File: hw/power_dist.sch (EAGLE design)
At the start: 78 parts, among them J1 JST-ZH6SMT_VERT, J2 JST-PH4SMT_VERT, J3 JST-PH5VERT, P1 XT30P, P2 XT30P, P3 XT30P, P4 XT30P, P5 XT30P, P6 XT30P, P7 XT90PW-M, Q1 PSMN4R8-100BSEJ, Q2 PSMN4R8-100BSEJ, Q3 PSMN4R8-100BSEJ, Q4 MF-DSC-SOT233-MMBT3904, Q5 MMBT5401 100V, U1 MAX15062AATA+T, U2 STM32G474CEU6, U4 TCAN334G, U5 LT1787HVIMS8PBF, U6 LTC4830

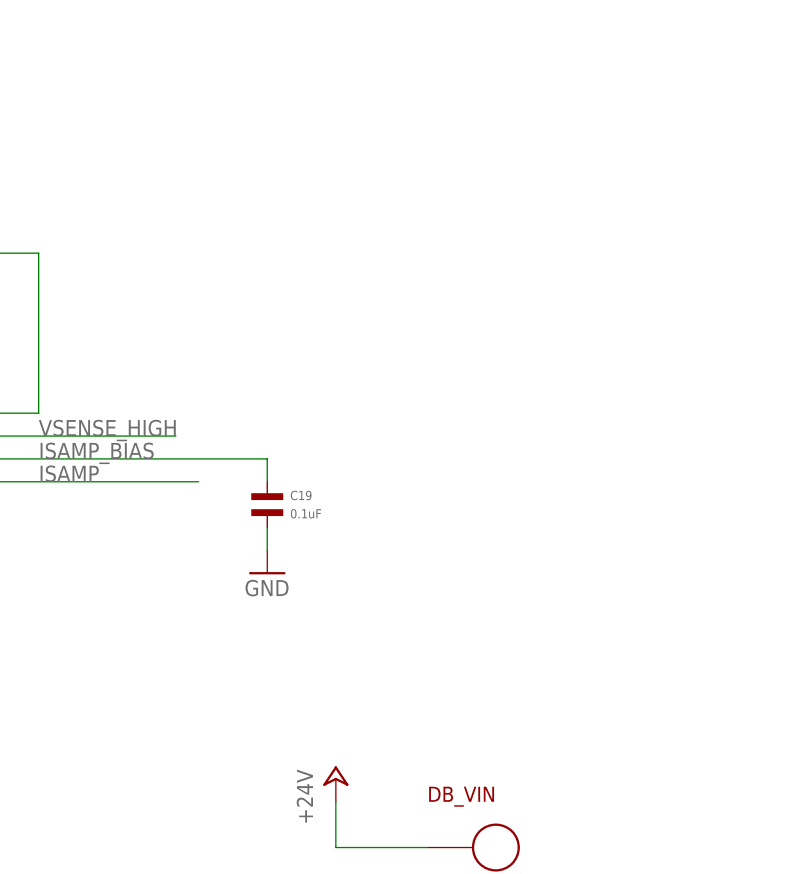
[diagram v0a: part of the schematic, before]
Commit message: Add more debugging pads
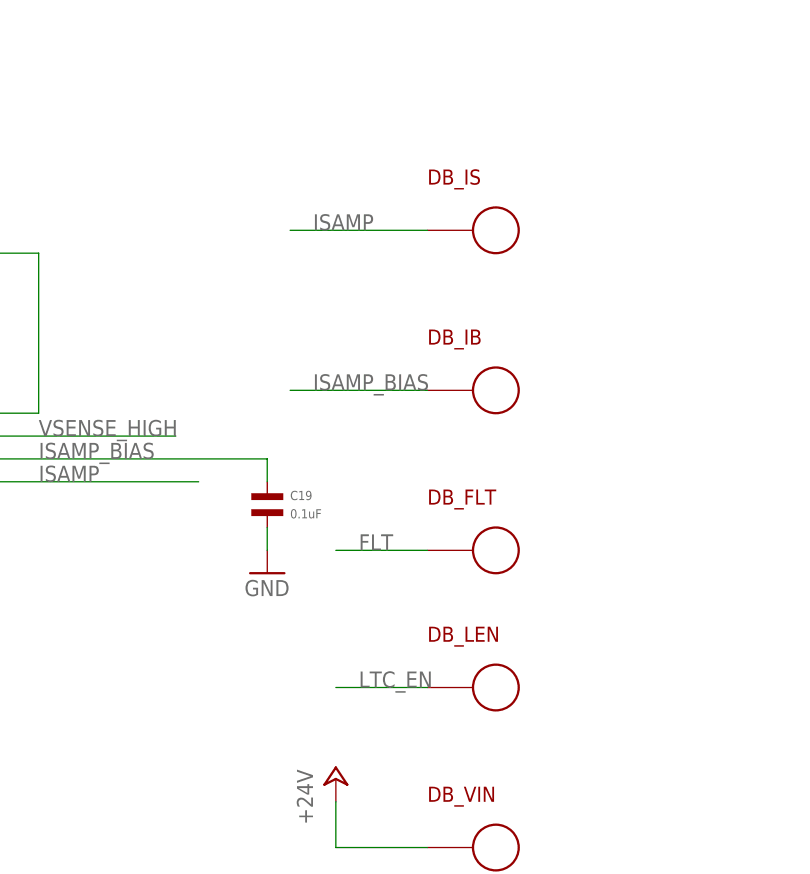
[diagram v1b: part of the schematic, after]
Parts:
- added DB_FLT, DB_IB, DB_IS, DB_LEN: PAD24AWG_PAD, precharge:PAD24AWG_PAD
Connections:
- net FLT: now also DB_FLT.P$1
- net ISAMP: now also DB_IS.P$1
- net ISAMP_BIAS: now also DB_IB.P$1
- net LTC_EN: now also DB_LEN.P$1
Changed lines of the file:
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@@
 <attribute name="MPN" value="MF-CAP-0603-0.01uF"/>
+</part>
+<part name="DB_LEN" library="precharge" deviceset="PAD" device="24AWG_PAD">
+<attribute name="POPULATE" value="0"/>
+</part>
+<part name="DB_FLT" library="precharge" deviceset="PAD" device="24AWG_PAD">
+<attribute name="POPULATE" value="0"/>
+</part>
+<part name="DB_IB" library="precharge" deviceset="PAD" device="24AWG_PAD">
+<attribute name="POPULATE" value="0"/>
+</part>
+<part name="DB_IS" library="precharge" deviceset="PAD" device="24AWG_PAD">
+<attribute name="POPULATE" value="0"/>
 </part>
 </parts>
@@
 <attribute name="VALUE" x="220.98" y="-44.704" size="1.016" layer="96" font="vector"/>
 </instance>
+<instance part="DB_LEN" gate="G$1" x="322.58" y="-7.62" smashed="yes">
+<attribute name="POPULATE" x="322.58" y="-7.62" size="1.778" layer="96" font="vector" display="off"/>
+<attribute name="NAME" x="314.96" y="-2.54" size="1.6764" layer="94"/>
+</instance>
+<instance part="DB_FLT" gate="G$1" x="322.58" y="7.62" smashed="yes">
+<attribute name="POPULATE" x="322.58" y="7.62" size="1.778" layer="96" font="vector" display="off"/>
+<attribute name="NAME" x="314.96" y="12.7" size="1.6764" layer="94"/>
+</instance>
+<instance part="DB_IB" gate="G$1" x="322.58" y="25.4" smashed="yes">
+<attribute name="POPULATE" x="322.58" y="25.4" size="1.778" layer="96" font="vector" display="off"/>
+<attribute name="NAME" x="314.96" y="30.48" size="1.6764" layer="94"/>
+</instance>
+<instance part="DB_IS" gate="G$1" x="322.58" y="43.18" smashed="yes">
+<attribute name="POPULATE" x="322.58" y="43.18" size="1.778" layer="96" font="vector" display="off"/>
+<attribute name="NAME" x="314.96" y="48.26" size="1.6764" layer="94"/>
+</instance>
 </instances>
 <busses>
@@
 <wire x1="454.66" y1="101.6" x2="454.66" y2="106.68" width="0.1524" layer="91"/>
 </segment>
+<segment>
+<pinref part="DB_FLT" gate="G$1" pin="P$1"/>
+<wire x1="314.96" y1="7.62" x2="304.8" y2="7.62" width="0.1524" layer="91"/>
+<label x="307.34" y="7.62" size="1.778" layer="95"/>
+</segment>
 </net>
 <net name="ISAMP_BIAS" class="0">
@@
 <label x="429.26" y="124.46" size="1.778" layer="95"/>
 </segment>
+<segment>
+<pinref part="DB_IB" gate="G$1" pin="P$1"/>
+<wire x1="314.96" y1="25.4" x2="299.72" y2="25.4" width="0.1524" layer="91"/>
+<label x="302.26" y="25.4" size="1.778" layer="95"/>
+</segment>
 </net>
 <net name="ISAMP" class="0">
@@
 <wire x1="477.52" y1="99.06" x2="523.24" y2="99.06" width="0.1524" layer="91"/>
 <label x="505.46" y="99.06" size="1.778" layer="95"/>
+</segment>
+<segment>
+<pinref part="DB_IS" gate="G$1" pin="P$1"/>
+<wire x1="314.96" y1="43.18" x2="299.72" y2="43.18" width="0.1524" layer="91"/>
+<label x="302.26" y="43.18" size="1.778" layer="95"/>
 </segment>
 </net>
@@
 <wire x1="520.7" y1="-50.8" x2="520.7" y2="-35.56" width="0.1524" layer="91"/>
 </segment>
-</net>
+<segment>
+<pinref part="DB_LEN" gate="G$1" pin="P$1"/>
+<wire x1="314.96" y1="-7.62" x2="304.8" y2="-7.62" width="0.1524" layer="91"/>
+<label x="307.34" y="-7.62" size="1.778" layer="95"/>
+</segment>
+</net>

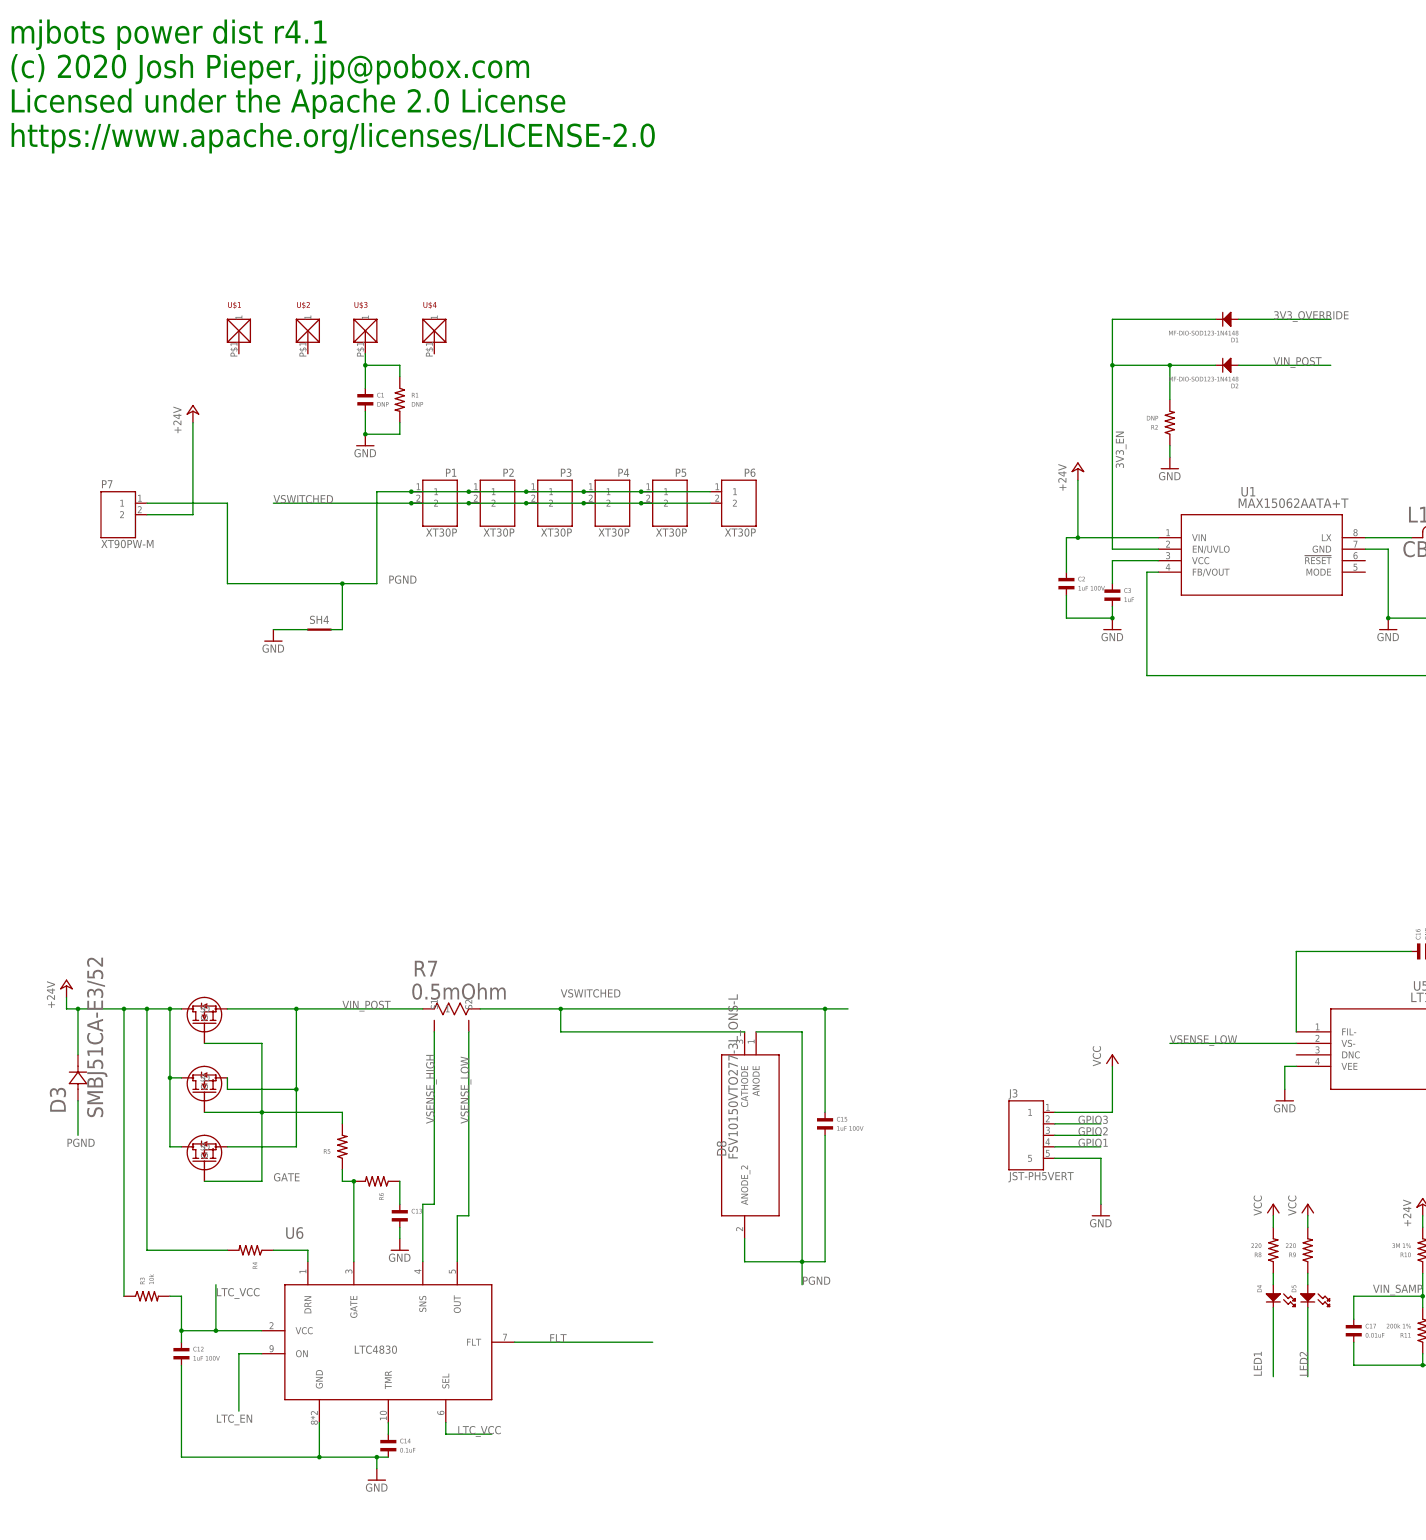
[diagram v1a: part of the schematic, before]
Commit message: Rough placement of r4.2 with the TPS2490
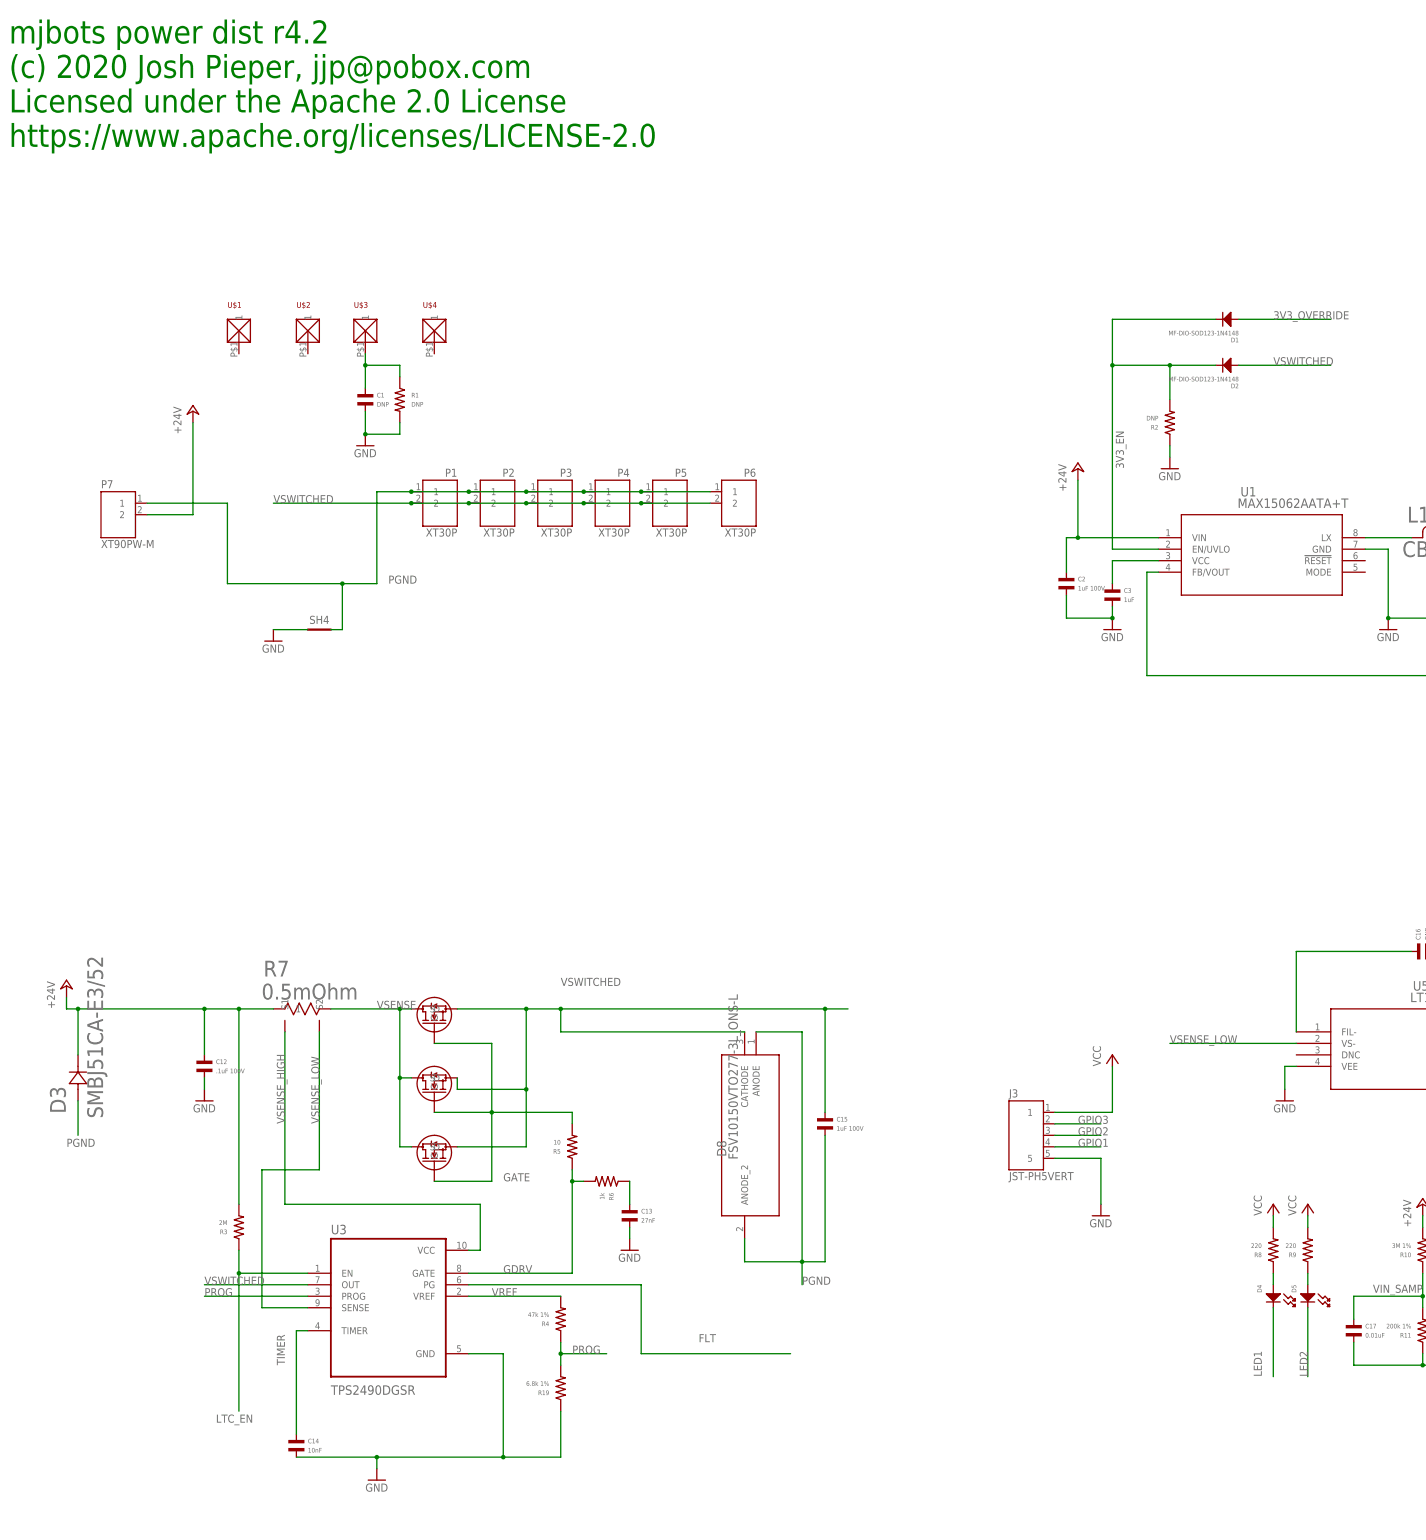
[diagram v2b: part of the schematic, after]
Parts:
- removed U6: LTC4830, power_dist:LTC4830
- added R19: 6.8k 1%, mfpassives:RESISTOR_0603
- added U3: TPS2490DGSR, TPS2490DGSR:TPS2490DGSR
- C12: value 1uF 100V -> .1uF 100V; device mfpassives:CAPACITOR_NP_0805 -> mfpassives:CAPACITOR_NP_0603; HOUSEPART (none) -> 1; MF MURATA -> (none); MPN GCM21BC72A105KE36L -> MF-CAP-0603-0.1uF
- C13: value (none) -> 27nF
- C14: value 0.1uF -> 10nF
- Q1, Q2, Q3: MANUFACTURER_PART_NUMBER (none) -> PSMN3R7-100BSE; MPN PSMN4R8-100BSEJ -> PSMN3R7-100BSE
- R3: value 10k -> 2M
- R4: value (none) -> 47k 1%
- R5: value (none) -> 10
- R6: value (none) -> 1k
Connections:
- removed net LTC_VCC: C12.P$1, R3.P$2, U6.SEL, U6.VCC
- removed net N$10: R4.P$1, U6.DRN
- removed net N$12: C14.P$1, U6.TMR
- removed net N$5: R5.P$1, R6.P$2, U6.GATE
- removed net VIN_POST: D2.ANODE, Q1.S, Q2.S, Q3.S, R7.1
- new net GDRV: R5.P$1, R6.P$2, U3.GATE
- new net PROG: R19.P$2, R4.P$1, U3.PROG
- new net TIMER: C14.P$1, U3.TIMER
- new net VREF: R4.P$2, U3.VREF
- new net VSENSE: Q1.D, Q2.D, Q3.D, R7.2
- net +24V: now also C12.P$1, R3.P$2, R7.1; no longer Q1.D, Q2.D, Q3.D, R3.P$1, R4.P$2
- net FLT: now also U3.PG; no longer U6.FLT
- net GND: now also R19.P$1, U3.GND; no longer U6.GND
- net LTC_EN: now also R3.P$1, U3.EN; no longer U6.ON
- net VSENSE_HIGH: now also U3.VCC; no longer U6.SNS
- net VSENSE_LOW: now also U3.SENSE; no longer U6.OUT
- net VSWITCHED: now also D2.ANODE, Q1.S, Q2.S, Q3.S, U3.OUT; no longer R7.2
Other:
- note added: "mjbots power dist r4.2 (c) 2020 Josh Pieper, jjp@pobox.com Licensed under the Apache 2.0 License https://www.apache.org/licenses/LICENSE-2.0"
- note removed: "mjbots power dist r4.1 (c) 2020 Josh Pieper, jjp@pobox.com Licensed under the Apache 2.0 License https://www.apache.org/licenses/LICENSE-2.0"
- moved on the sheet: C12, C13, C14, R3, R4, R5, R6, R7

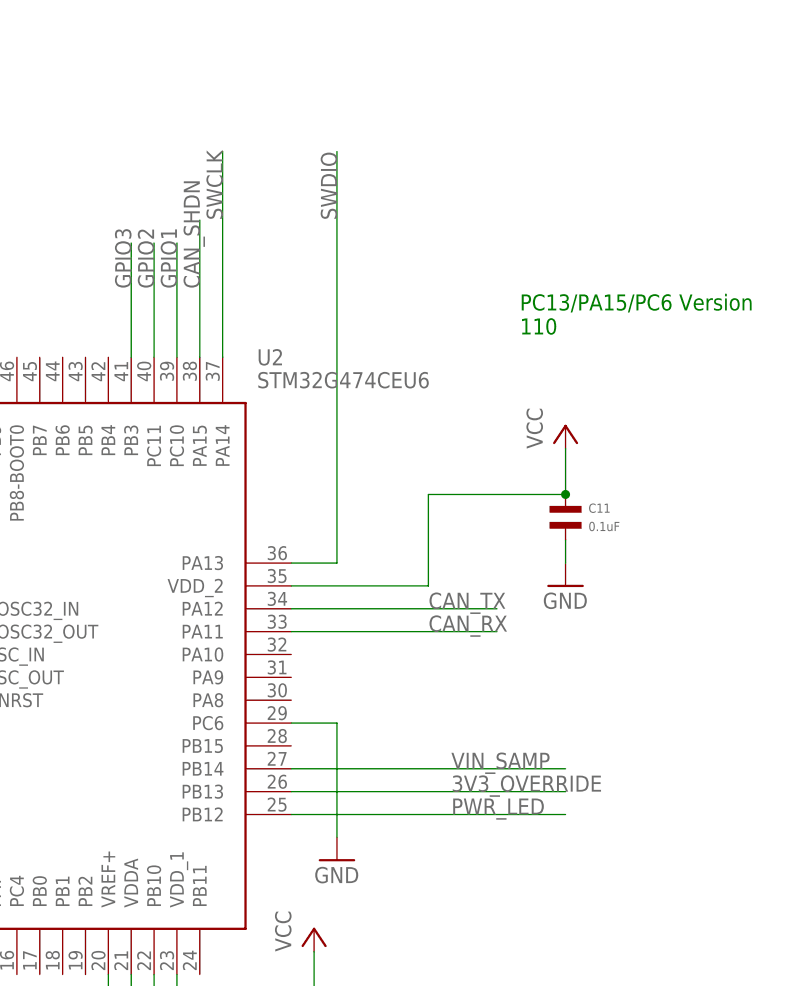
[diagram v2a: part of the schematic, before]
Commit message: r4.2 everything rough routed
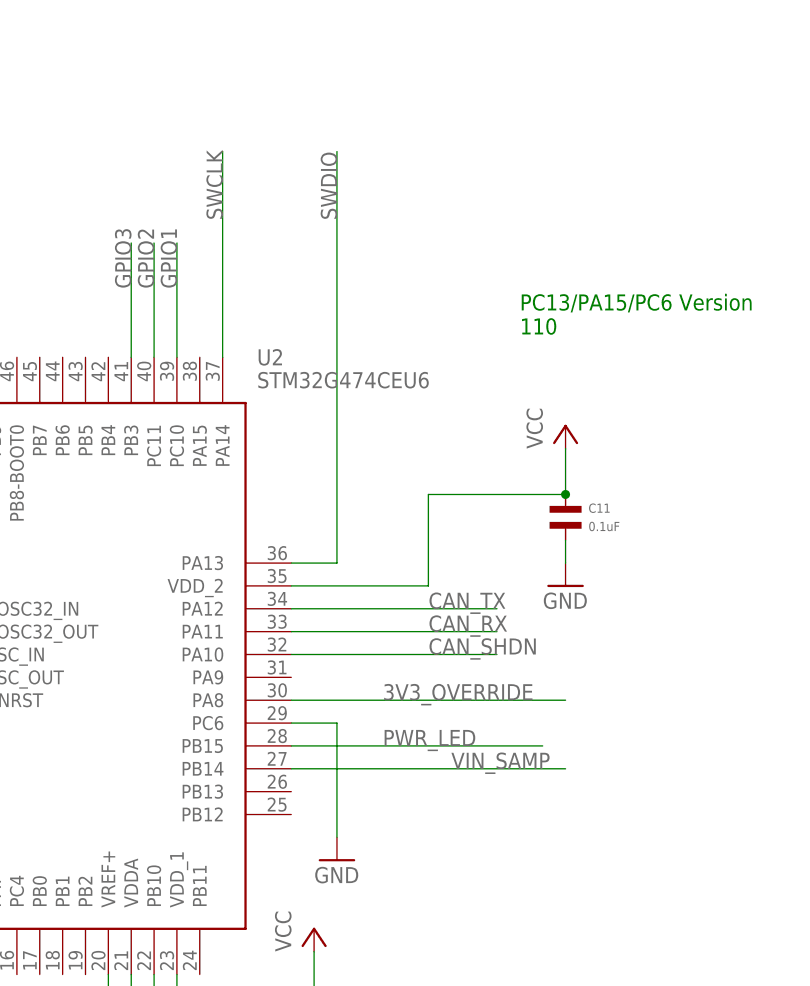
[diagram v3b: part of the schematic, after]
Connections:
- net 3V3_OVERRIDE: now also U2.PA8; no longer U2.PB13
- net CAN_SHDN: now also U2.PA10; no longer U2.PA15
- net PWR_LED: now also U2.PB15; no longer U2.PB12
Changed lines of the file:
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@@
 </segment>
 <segment>
-<pinref part="U2" gate="G$1" pin="PA15"/>
-<wire x1="482.6" y1="175.26" x2="482.6" y2="190.5" width="0.1524" layer="91"/>
-<label x="482.6" y="182.88" size="1.778" layer="95" rot="R90"/>
+<pinref part="U2" gate="G$1" pin="PA10"/>
+<wire x1="492.76" y1="142.24" x2="515.62" y2="142.24" width="0.1524" layer="91"/>
+<label x="508" y="142.24" size="1.778" layer="95"/>
 </segment>
 </net>
@@
 </segment>
 <segment>
-<pinref part="U2" gate="G$1" pin="PB12"/>
-<wire x1="492.76" y1="124.46" x2="523.24" y2="124.46" width="0.1524" layer="91"/>
-<label x="510.54" y="124.46" size="1.778" layer="95"/>
+<pinref part="U2" gate="G$1" pin="PB15"/>
+<wire x1="492.76" y1="132.08" x2="520.7" y2="132.08" width="0.1524" layer="91"/>
+<label x="502.92" y="132.08" size="1.778" layer="95"/>
 </segment>
 </net>
@@
 </segment>
 <segment>
-<pinref part="U2" gate="G$1" pin="PB13"/>
-<wire x1="492.76" y1="127" x2="523.24" y2="127" width="0.1524" layer="91"/>
-<label x="510.54" y="127" size="1.778" layer="95"/>
-</segment>
-</net>
+<pinref part="U2" gate="G$1" pin="PA8"/>
+<wire x1="492.76" y1="137.16" x2="523.24" y2="137.16" width="0.1524" layer="91"/>
+<label x="502.92" y="137.16" size="1.778" layer="95"/>
+</segment>
+</net>
